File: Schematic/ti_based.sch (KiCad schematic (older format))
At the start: 37 parts, among them P1 HE10-10

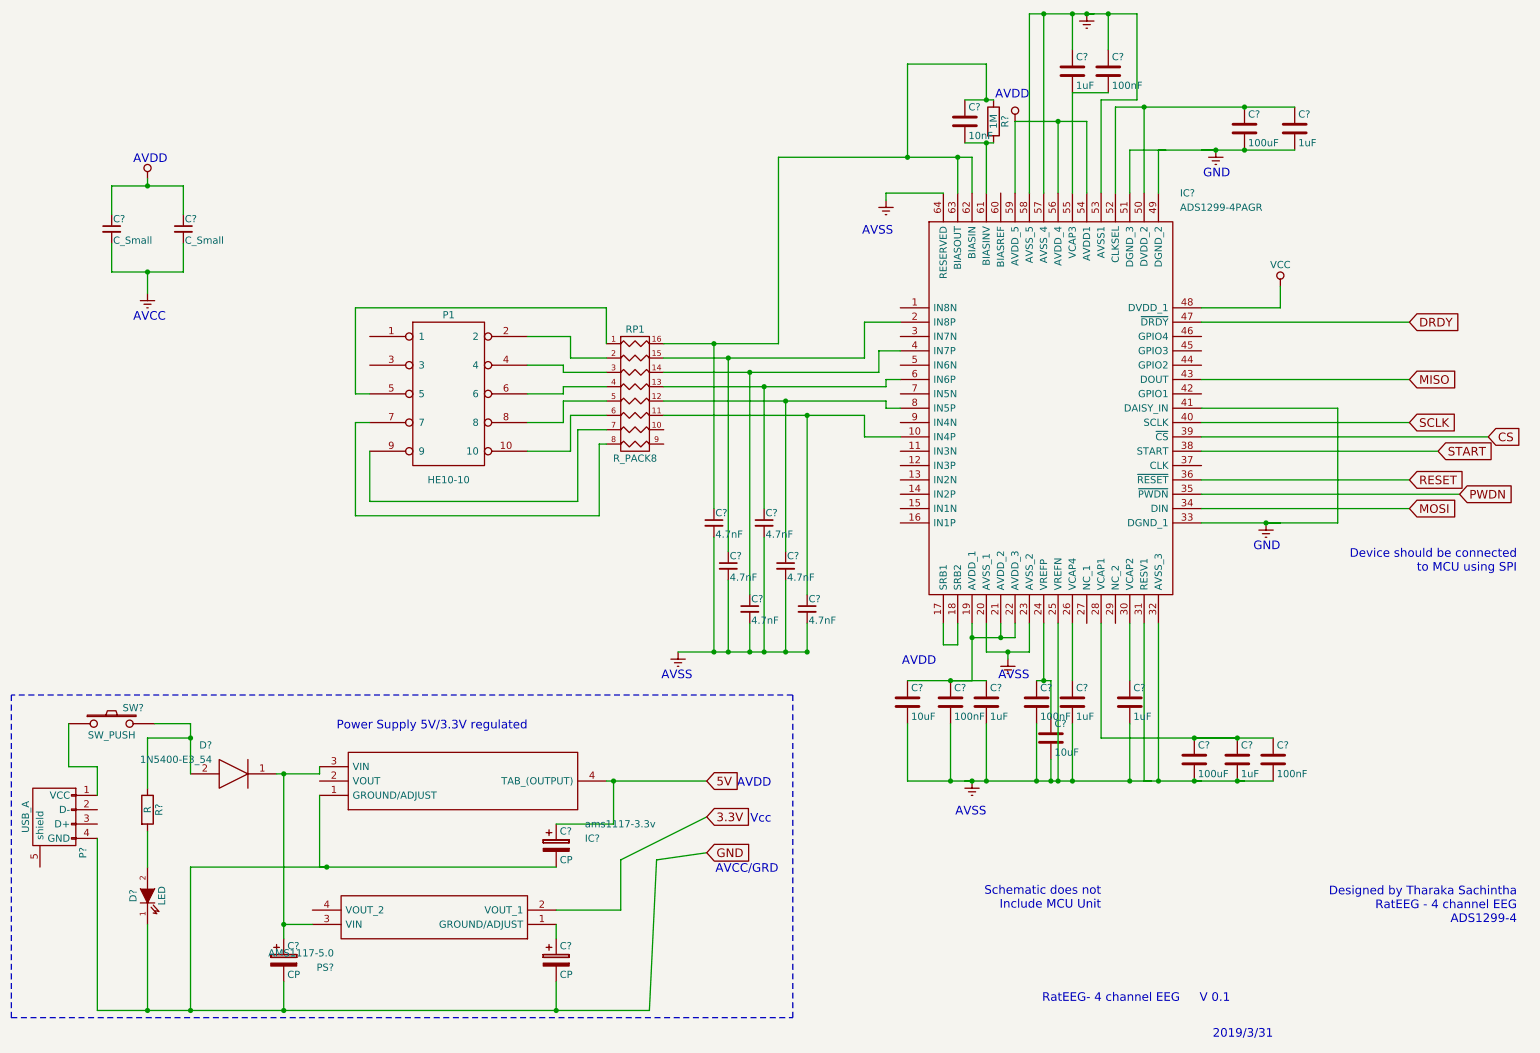
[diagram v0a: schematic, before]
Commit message: added detailed schematics
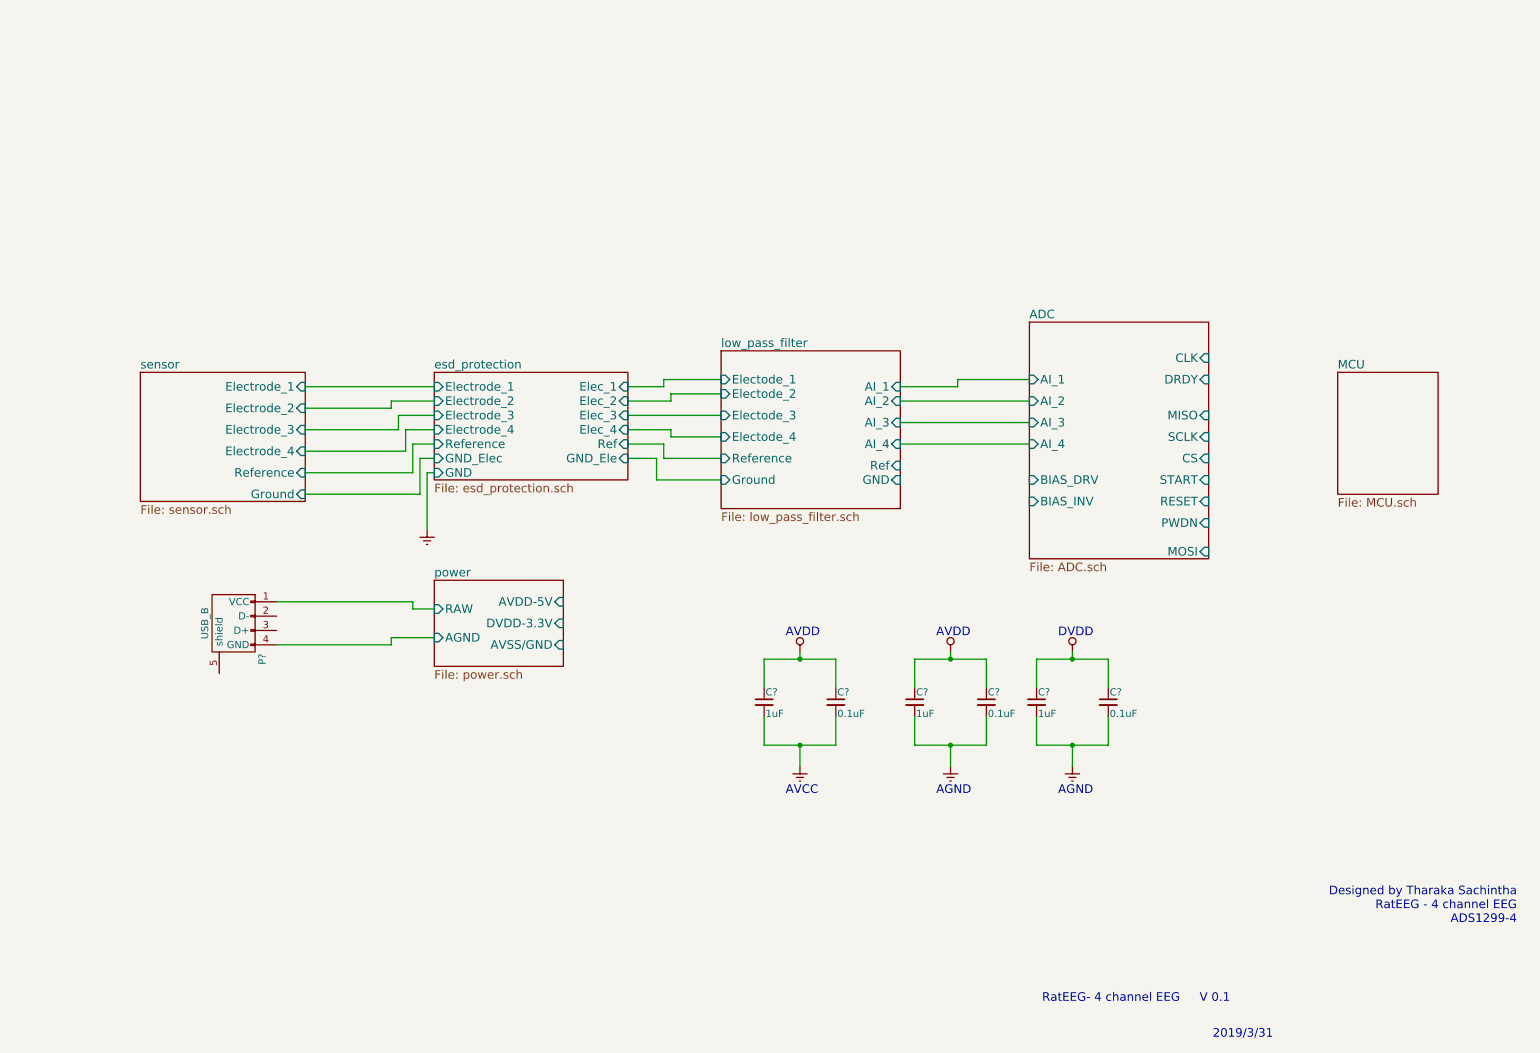
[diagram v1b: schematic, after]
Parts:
- removed C? (x2): 10uF, symbol C
- removed C? (x4): 100nF, symbol C
- removed C? (x6): 1uF, symbol C
- removed C? (x2): 100uF, symbol C
- removed C?: 10nF, symbol C
- removed C? (x3): CP, symbol CP
- removed C? (x6): 4.7nF, symbol C_Small
- removed D?: LED, symbol LED
- removed D?: 1N5400-E3_54, DIOAD2855W132L835D505, symbol 1N5400-E3_54
- removed IC?: ADS1299-4PAGR, QFP50P1200X1200X120-64N, symbol ADS1299-4PAGR
- removed IC?: ams1117-3.3v, SOT229P700X180-4N, symbol ams1117-3.3v
- removed P1: HE10-10, symbol HE10-10
- removed P?: USB_A, symbol USB_A
- removed PS?: AMS1117-5.0, SOT229P700X180-4N, symbol AMS1117-5.0
- removed R?: R, symbol R
- removed R?: 1M, symbol R
- removed RP1: R_PACK8, symbol R_PACK8
- removed SW?: SW_PUSH, symbol SW_PUSH
- added C? (x2): 1uF, symbol C_Small
- added C? (x2): 0.1uF, symbol C_Small
- added P?: USB_B, symbol USB_B
- C?: value C_Small -> 1uF
- C?: value C_Small -> 0.1uF
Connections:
- net labels removed: 3.3V, 5V, CS, DRDY, GND, MISO, MOSI, PWDN, RESET, SCLK, START, VCC
- wire segments 180 -> 76
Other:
- note added: "AGND\n"
- note added: "DVDD\n"
- note removed: "AVCC/GRD"
- note removed: "AVDD"
- note removed: "AVSS"
- note removed: "AVSS\n"
- note removed: "Device should be connected \nto MCU using SPI"
- note removed: "GND"
- note removed: "Power Supply 5V/3.3V regulated\n"
- note removed: "Schematic does not\nInclude MCU Unit\n"
- note removed: "Vcc\n"
- moved on the sheet: C?
